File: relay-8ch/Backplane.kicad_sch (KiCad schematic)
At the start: 18 parts, among them J201 Backplane, U201 AT24CS32-SSHM, U202 ATF22V10C

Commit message: Finished routing relay board
- Completed routing of the relay board; it's got added an address
  selector switch and an I2C expander that can be used to set the
  address automatically.

- Minor tweaks to a few footprints, namely to make sure they're
  correctly tagged as through hole/SMD
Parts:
- removed R202: 10k, Resistor_SMD:R_0805_2012Metric, symbol Device:R_Small
- added C211: 100nF, Capacitor_SMD:C_0805_2012Metric, symbol Device:C_Small
- added RN201, RN202: 10k, Resistor_THT:R_Array_SIP5, symbol Device:R_Network04
- added SW201, SW202: SW_Coded_SH-7050, Button_Switch_THT:Nidec_Copal_SH-7010C, symbol Switch:SW_Coded_SH-7050
- added U203: MCP23008-xSO, Package_SO:SOIC-18W_7.5x11.6mm_P1.27mm, symbol Interface_Expansion:MCP23008-xSO
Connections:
- net +5V: now also C211.2, SW201.C, SW202.C, U203.18 (VDD), U203.3 (A2)
- net GND: now also C211.1, RN201.1 (common), RN202.1 (common), U203.4 (A1), U203.5 (A0), U203.9 (VSS)
- net I2C_SCL: now also U203.1 (SCL)
- net I2C_SDA: now also U203.2 (SDA)
- net ~{RESET}: now also U203.6 (~{RESET})
- net SET0: now reaches U202.10 (IN10)
- net SET0: now also RN201.3 (R2), SW202.1, U203.16 (GP6)
- net SET3: now reaches U202.15 (IO2)
- net SET3: now also RN201.2 (R1), SW202.8, U203.17 (GP7)
- net SET1: now reaches U202.16 (IO3)
- net SET1: now also RN201.4 (R3), SW202.2, U203.15 (GP5)
- net SET7: now reaches U202.17 (IO4)
- net SET7: now also RN202.5 (R4), SW201.8, U203.13 (GP3)
- net SET4: now reaches U202.18 (IO5)
- net SET4: now also RN202.4 (R3), SW201.1, U203.12 (GP2)
- net SET5: now reaches U202.19 (IO6)
- net SET5: now also RN202.3 (R2), SW201.2, U203.11 (GP1)
- net SET6: now reaches U202.20 (IO7)
- net SET6: now also RN202.2 (R1), SW201.4, U203.10 (GP0)
- net SET2: now reaches U202.9 (IN9)
- net SET2: now also RN201.5 (R4), SW202.4, U203.14 (GP4)
- no-connect marks 4 -> 5
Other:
- note added: "Address: 0b0100100"
- note added: "TODO: check function codes; generate DTACK"

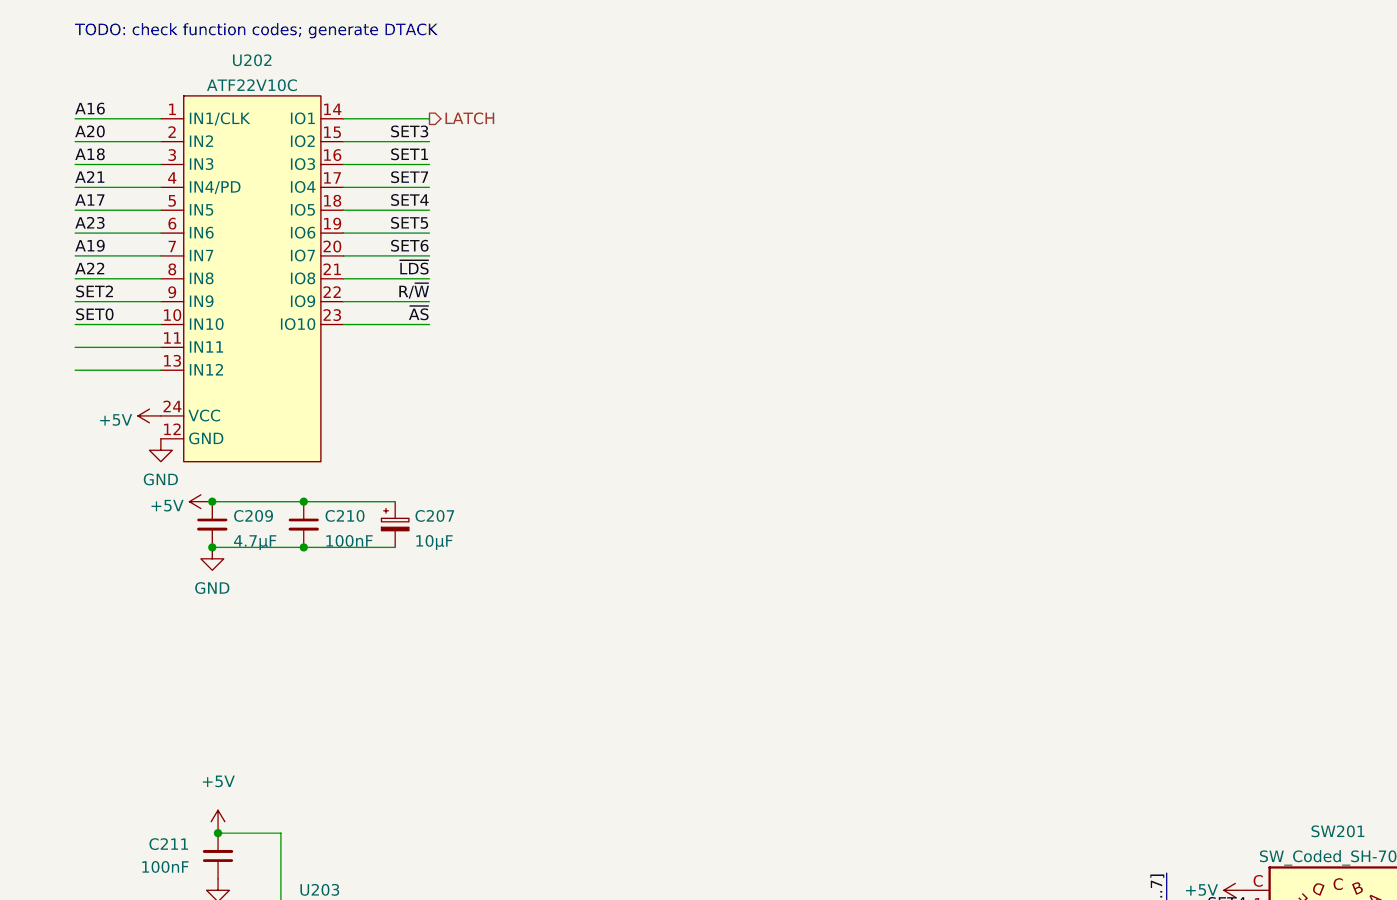
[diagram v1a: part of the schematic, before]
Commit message: Function codes, /DTACK for relay board
- Consider the state of the function code signals (so we don't decode
  CPU space cycles as accesses) and assert /DTACK when the latch signal
  is asserted. This should work for bus speeds of up to around 16MHz
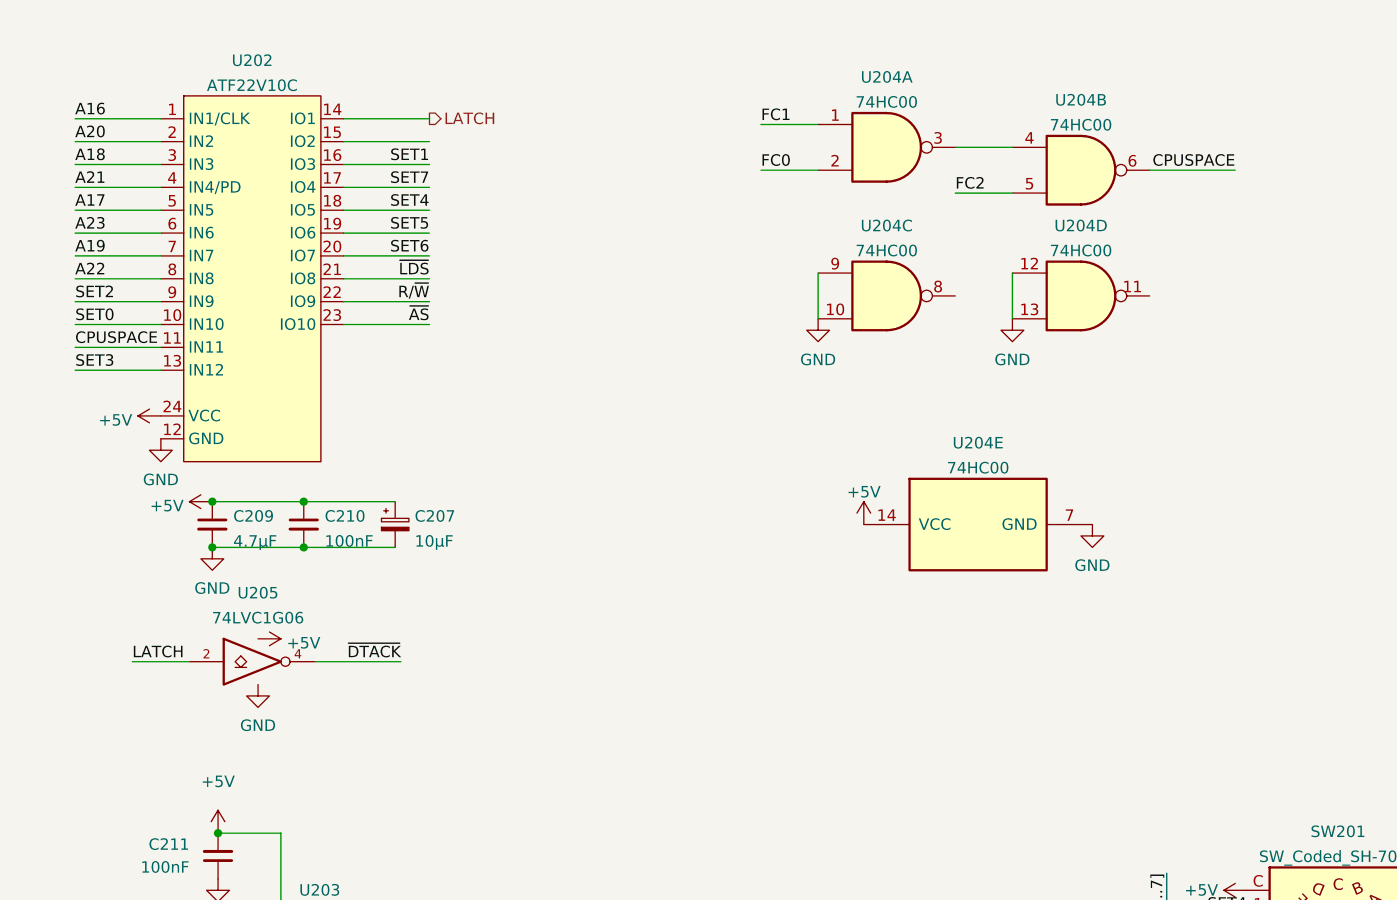
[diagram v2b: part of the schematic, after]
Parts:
- added U204: 74HC00, Package_SO:SOIC-14_3.9x8.7mm_P1.27mm, symbol 74xx:74HC00
- added U205: 74LVC1G06, 68komputer-common:SC-74-5_1.5x2.9mm_P0.95mm, symbol 74xGxx:74LVC1G06
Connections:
- net +5V: now also U204.14 (VCC), U205.5 (VCC)
- net FC0: now also U204.2
- net FC1: now also U204.1
- net FC2: now also U204.5
- net GND: now also U204.10, U204.12, U204.13, U204.7 (GND), U204.9, U205.3 (GND)
- net LATCH: now also U205.2
- net SET3: now also U202.13 (IN12); no longer U202.15 (IO2)
- net ~{DTACK}: now also U205.4
- net CPUSPACE: now reaches U202.11 (IN11)
- net CPUSPACE: now also U204.6
- new net: U204.3, U204.4
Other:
- note removed: "TODO: check function codes; generate DTACK"
- title: (none) -> 8 Channel Relay IO

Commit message: Minor tweaks to all boards
- Moved around some traces on the 68000 CPU card for prettiness

- Added a connector on the backplane to provide +5V/+12V without a
  management card installed (for testing)
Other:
- company: (none) -> Tristan Seifert
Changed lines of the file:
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@@
   (title_block
     (title "8 Channel Relay IO")
-    (date "2022-01-08")
+    (date "2022-01-09")
     (rev "1")
+    (company "Tristan Seifert")
   )
   (junction (at 217.805 27.305) (diameter 0) (color 0 0 0 0)

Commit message: Tweaks to bill of materials
- Added missing MPN's for a few components; tweaked a few bits of layout
  to increase some tolerances

  This includes kind of tweaking the boot rom socket positions in hopes
  of fitting fancier sockets
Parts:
- JP201: now left out of the parts list
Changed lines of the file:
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@@
   )
   (symbol (lib_id "Jumper:Jumper_3_Bridged12") (at 60.96 178.435 270) (mirror x) (unit 1)
-    (in_bom yes) (on_board yes) (fields_autoplaced)
+    (in_bom no) (on_board yes) (fields_autoplaced)
     (property "Reference" "JP201" (id 0) (at 62.611 177.5265 90)
       (effects (font (size 1.27 1.27)) (justify left))

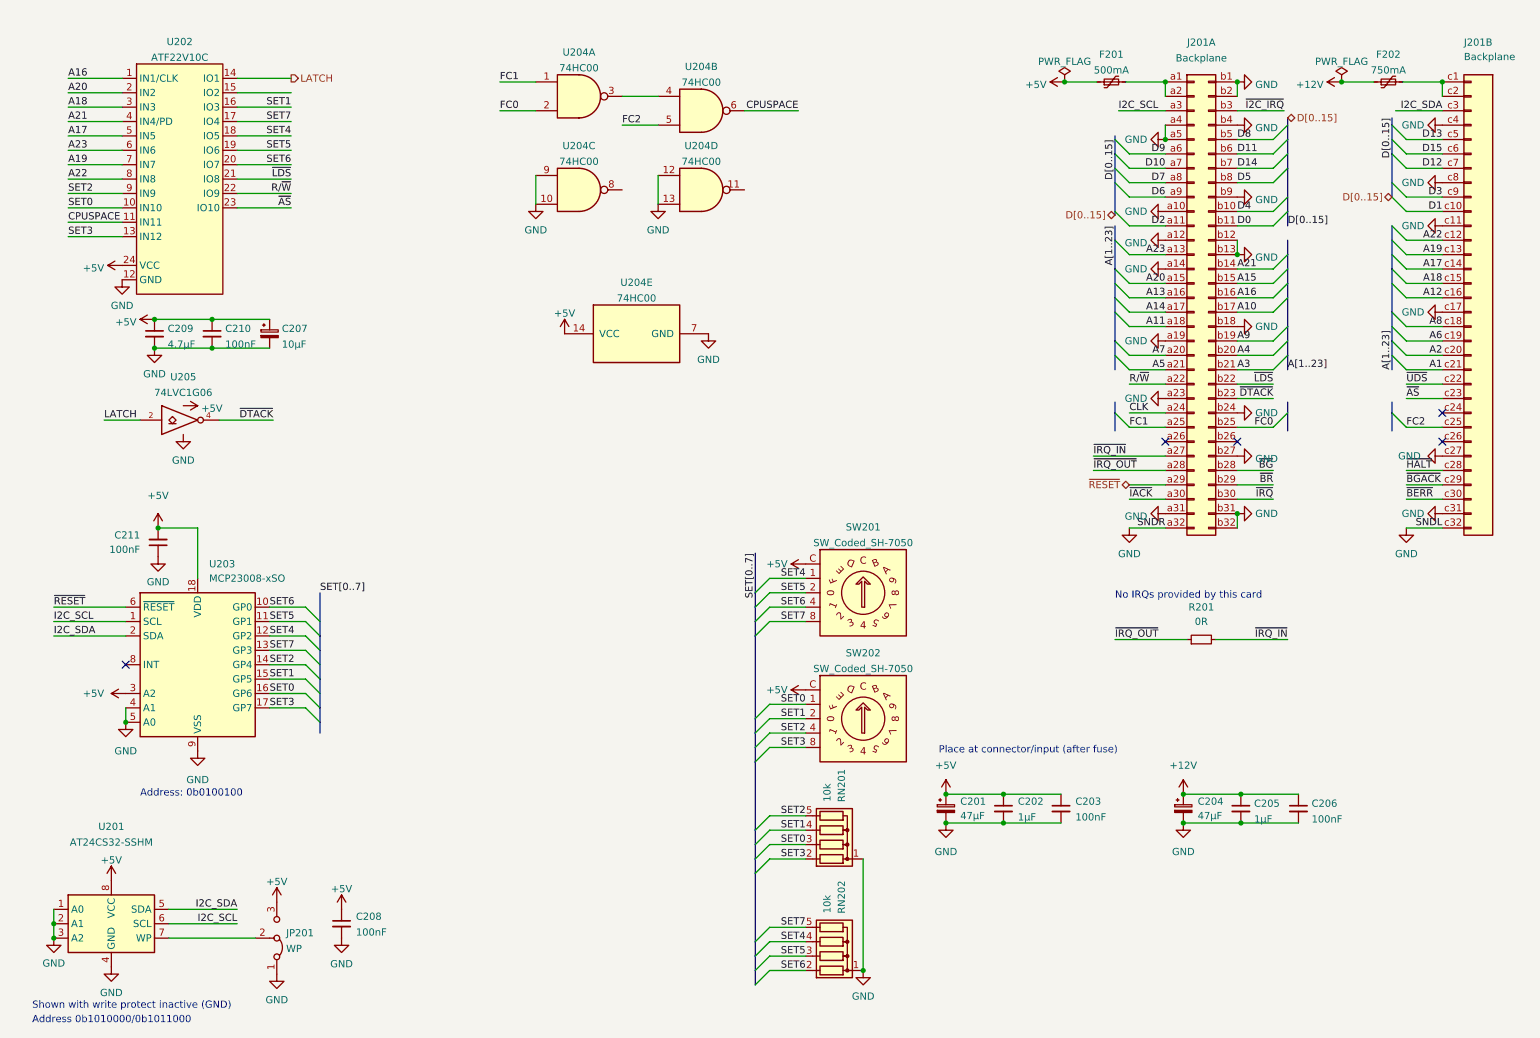
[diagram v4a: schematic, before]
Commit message: Removed GAL from relay board
- Replaced the GAL on the relay board with some hard 74-series logic;
  this means the board needs zero "hard to get" parts.

  All the address decoding is done by a '688 magnitude comparison IC,
  which is LS logic so this board needs to consist of HCT logic to deal
  with its lower active high level.

- Replaced 3D model for the hexadecimal rotary switches to one that has
  color :D
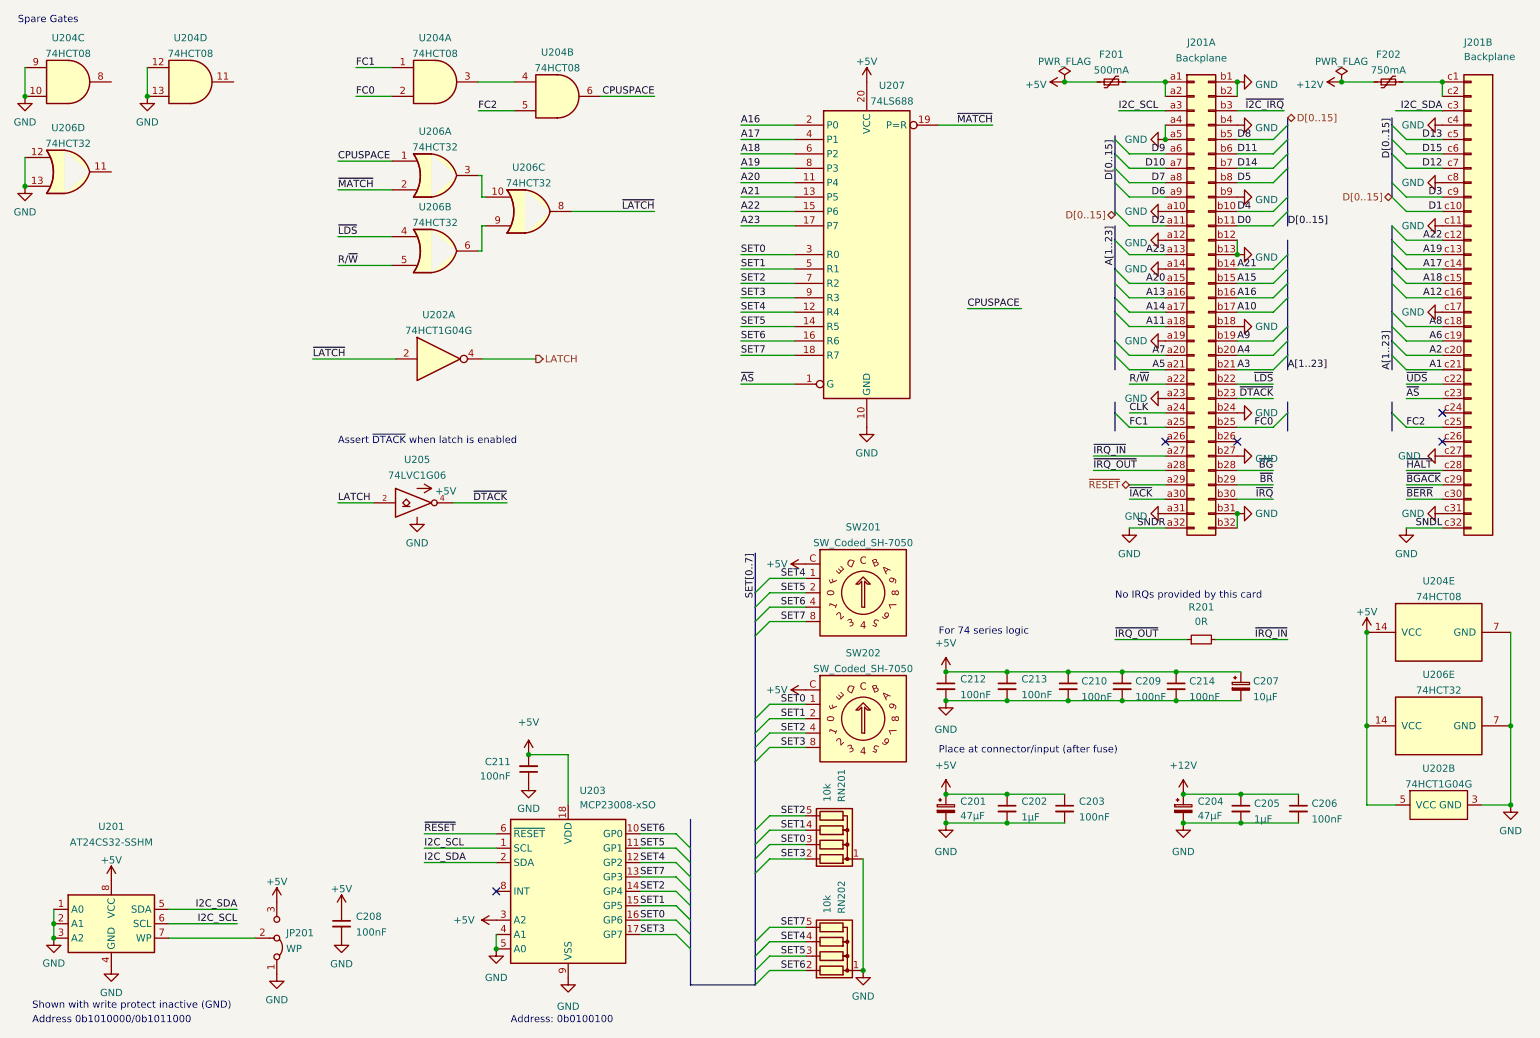
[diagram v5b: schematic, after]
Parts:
- removed U202: ATF22V10C, Package_DIP:DIP-24_W7.62mm_Socket, symbol 68komputer-common:ATF22V10C
- added C212, C213, C214: 100nF, Capacitor_SMD:C_0805_2012Metric, symbol Device:C_Small
- added U202: 74HCT1G04G, 68komputer-common:SC-74-5_1.5x2.9mm_P0.95mm, symbol 68komputer-common:74HCT1G04G
- added U206: 74HCT32, Package_SO:SO-14_3.9x8.65mm_P1.27mm, symbol 74xx:74LS32
- added U207: 74LS688, Package_SO:SOIC-20W_7.5x12.8mm_P1.27mm, symbol 74xx:74LS688
- C209: value 4.7µF -> 100nF
- U204: value 74HC00 -> 74HCT08; footprint Package_SO:SOIC-14_3.9x8.7mm_P1.27mm -> Package_SO:SO-14_3.9x8.65mm_P1.27mm; symbol 74xx:74HC00 -> 74xx:74LS08
- U204: value 74HC00 -> 74HCT08; footprint Package_SO:SOIC-14_3.9x8.7mm_P1.27mm -> Package_SO:SO-14_3.9x8.65mm_P1.27mm; symbol 74xx:74HC00 -> 74xx:74LS08; MPN 74HC00D,653 -> 74HCT08S14-13
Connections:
- net +5V: now also C212.1, C213.1, C214.1, U202.5 (VCC), U206.14 (VCC), U207.20 (VCC)
- net A16: now also U207.2 (P0)
- net A17: now also U207.4 (P1)
- net A18: now also U207.6 (P2)
- net A19: now also U207.8 (P3)
- net A20: now also U207.11 (P4)
- net A21: now also U207.13 (P5)
- net A22: now also U207.15 (P6)
- net A23: now also U207.17 (P7)
- net CPUSPACE: now also U206.1
- net GND: now also C212.2, C213.2, C214.2, U202.3 (GND), U206.12, U206.13, U206.7 (GND), U207.10 (GND)
- net LATCH: now also U202.4
- net R/~{W}: now also U206.5
- net SET0: now also U207.3 (R0)
- net SET1: now also U207.5 (R1)
- net SET2: now also U207.7 (R2)
- net SET3: now also U207.9 (R3)
- net SET4: now also U207.12 (R4)
- net SET5: now also U207.14 (R5)
- net SET6: now also U207.16 (R6)
- net SET7: now also U207.18 (R7)
- net ~{AS}: now also U207.1 (G)
- net ~{LDS}: now also U206.4
- new net: U206.10, U206.3
- new net: U206.6, U206.9
- new net ~{LATCH}: U202.2, U206.8
- new net ~{MATCH}: U206.2, U207.19 (P=R)
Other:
- note added: "Assert ~{DTACK} when latch is enabled"
- note added: "For 74 series logic"
- note added: "Spare Gates"
- moved on the sheet: C202, C203, C207, C210, C211, U203, U204E, U205

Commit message: Minor tweaks based from assembly
- Replaced the AT24CS32 EEPROMs with the AT24CS16 which is what was
  ordered. These are half the size, but use a totally different
  addressing scheme which needs to be followed. So, we should just
  standardize on these.

  The information stored in the actual EEPROM section (2KBytes in this
  part) will likely not be much larger than a small 32 byte (or so)
  header.

- Removed a few redundant parts on the power management board, namely
  some resistors

- Fixed the fucked footprint for the PTH08T220WAD module; the annular
  rings were way too small
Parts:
- U201: value AT24CS32-SSHM -> AT24CS16-SSHM; symbol Memory_EEPROM:AT24CS32-SSHM -> Memory_EEPROM:AT24CS16-SSHM
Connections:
- net GND: no longer U201.1 (A0), U201.2 (A1), U201.3 (A2)
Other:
- note added: "Address 0b1010xxx/0b1011000"
- note removed: "Address 0b1010000/0b1011000"
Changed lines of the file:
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@@
   (junction (at 219.71 131.445) (diameter 0) (color 0 0 0 0)
   )
-  (junction (at 21.59 175.895) (diameter 0) (color 0 0 0 0)
-  )
   (junction (at 105.41 146.05) (diameter 0) (color 0 0 0 0)
   )
@@
   )
   (junction (at 179.07 131.445) (diameter 0) (color 0 0 0 0)
-  )
-  (junction (at 21.59 178.435) (diameter 0) (color 0 0 0 0)
   )
   (junction (at 278.765 154.94) (diameter 0) (color 0 0 0 0)
@@
     (stroke (width 0) (type default) (color 0 0 0 0))
   )
-  (wire (pts (xy 21.59 173.355) (xy 21.59 175.895))
-    (stroke (width 0) (type default) (color 0 0 0 0))
-  )
   (bus (pts (xy 133.985 180.34) (xy 133.985 186.69))
     (stroke (width 0) (type default) (color 0 0 0 0))
@@
     (stroke (width 0) (type default) (color 0 0 0 0))
   )
-  (wire (pts (xy 21.59 175.895) (xy 21.59 178.435))
-    (stroke (width 0) (type default) (color 0 0 0 0))
-  )
   (bus (pts (xy 145.415 144.78) (xy 145.415 147.32))
     (stroke (width 0) (type default) (color 0 0 0 0))
@@
     (effects (font (size 1.27 1.27)) (justify left bottom))
   )
-  (text "Address 0b1010000/0b1011000" (at 17.78 193.675 0)
+  (text "Address 0b1010xxx/0b1011000" (at 17.78 193.675 0)
     (effects (font (size 1.27 1.27)) (justify left bottom))
   )
@@
     (pin "1")
   )
-  (symbol (lib_id "power:GND") (at 21.59 178.435 0) (unit 1)
-    (in_bom yes) (on_board yes) (fields_autoplaced)
-    (property "Reference" "#PWR0105" (id 0) (at 21.59 184.785 0)
-      (effects (font (size 1.27 1.27)) hide)
-    )
-    (property "Value" "GND" (id 1) (at 21.59 182.88 0))
-    (property "Footprint" "" (id 2) (at 21.59 178.435 0)
-      (effects (font (size 1.27 1.27)) hide)
-    )
-    (property "Datasheet" "" (id 3) (at 21.59 178.435 0)
-      (effects (font (size 1.27 1.27)) hide)
-    )
-    (pin "1")
-  )
   (symbol (lib_id "Interface_Expansion:MCP23008-xSO") (at 112.395 170.18 0) (unit 1)
     (in_bom yes) (on_board yes) (fields_autoplaced)
@@
     (pin "1")
   )
-  (symbol (lib_id "Memory_EEPROM:AT24CS32-SSHM") (at 31.75 175.895 0) (unit 1)
+  (symbol (lib_id "Memory_EEPROM:AT24CS16-SSHM") (at 31.75 175.895 0) (unit 1)
     (in_bom yes) (on_board yes)
     (property "Reference" "U201" (id 0) (at 31.75 158.75 0))
-    (property "Value" "AT24CS32-SSHM" (id 1) (at 31.75 161.5251 0))
+    (property "Value" "AT24CS16-SSHM" (id 1) (at 34.29 182.245 0)
+      (effects (font (size 1.27 1.27)) (justify left))
+    )
     (property "Footprint" "Package_SO:SOIC-8_3.9x4.9mm_P1.27mm" (id 2) (at 31.75 175.895 0)
       (effects (font (size 1.27 1.27)) hide)
     )
-    (property "Datasheet" "http://ww1.microchip.com/downloads/en/DeviceDoc/Atmel-8869-SEEPROM-AT24CS32-Datasheet.pdf" (id 3) (at 31.75 175.895 0)
+    (property "Datasheet" "http://ww1.microchip.com/downloads/en/DeviceDoc/Atmel-8859-SEEPROM-AT24CS16-Datasheet.pdf" (id 3) (at 31.75 175.895 0)
       (effects (font (size 1.27 1.27)) hide)
     )
@@
       (effects (font (size 1.27 1.27)) hide)
     )
-    (pin "1")
-    (pin "2")
-    (pin "3")
     (pin "4")
     (pin "5")
